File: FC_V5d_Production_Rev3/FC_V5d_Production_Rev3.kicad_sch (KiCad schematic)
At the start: 77 parts, among them IC3 RV-3028-C7_32.768kHz_1ppm_TA_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, J12 USB_C_Receptacle_USB2.0_16P, J16 DEBUG, J18 Payload, J22 SWD Port, J3 Life Makes Lemonade, J5 BM04B-SRSS-TB(LF)(SN), SW1 KMR2, SW2 KMR2, U12 TCA9548ARGERQ1, U14 TCA4307DGKR, U15 LIS2MDL, U2 ZDSD04GLGEAG, U30 E28-2G4M27S, U4 RFM98PW, U7 LSM6DSOTR

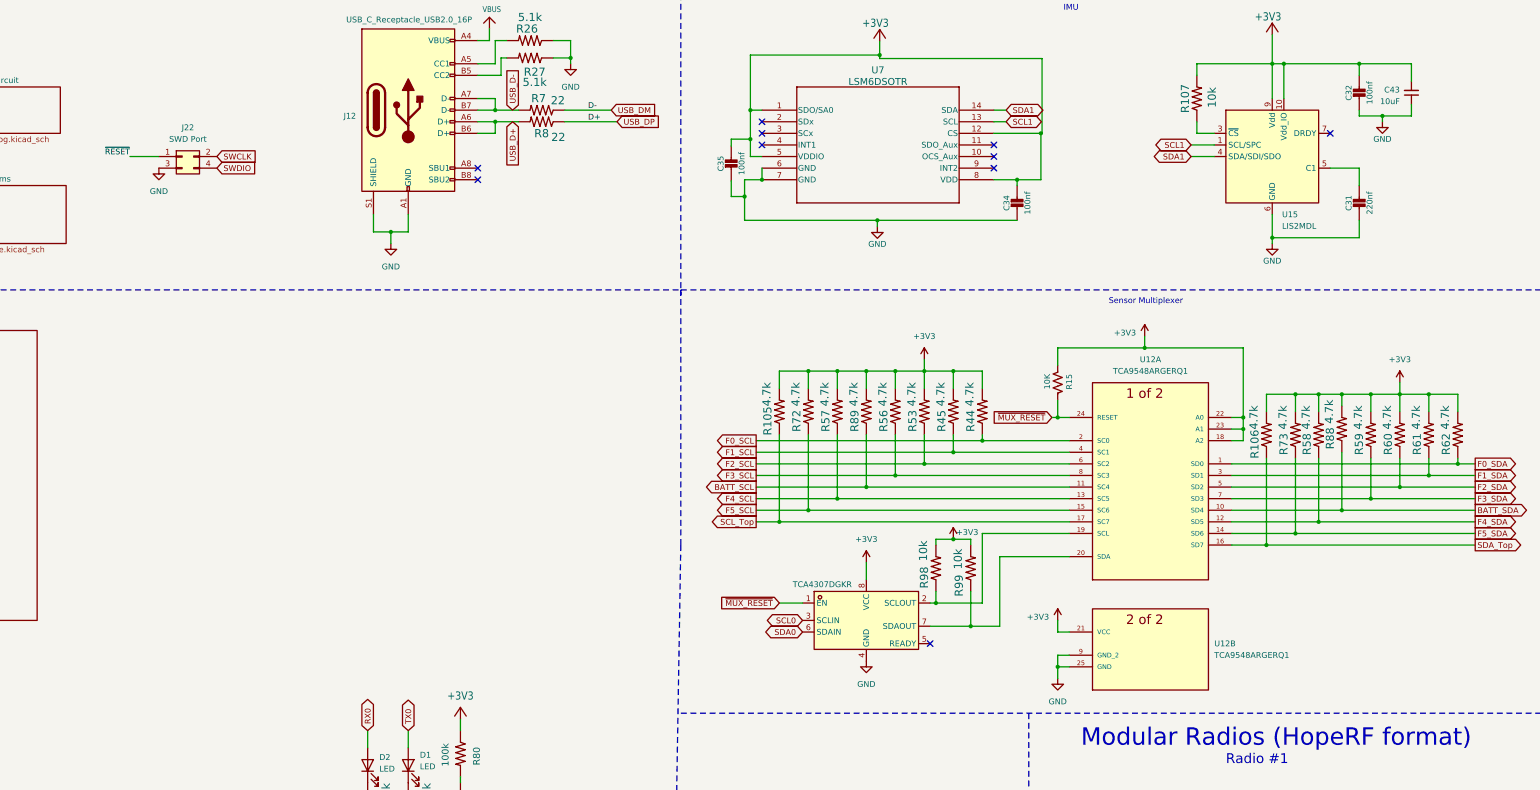
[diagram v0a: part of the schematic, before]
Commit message: Swapped to TCA With Leads
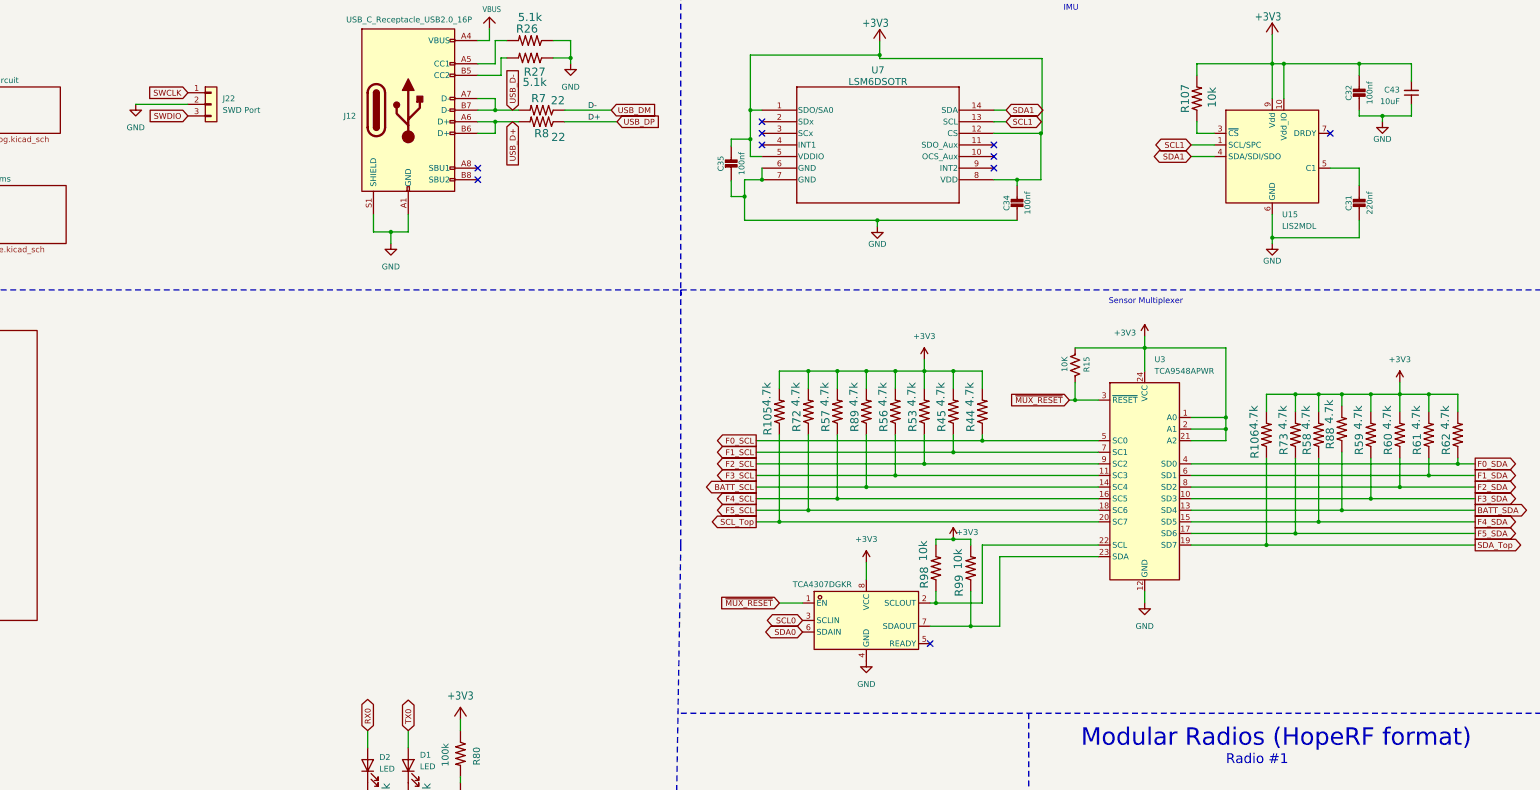
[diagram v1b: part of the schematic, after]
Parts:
- removed J22: SWD Port, Connector_PinHeader_1.27mm:PinHeader_2x02_P1.27mm_Vertical, symbol Connector_Generic:Conn_02x02_Odd_Even
- removed U12: TCA9548ARGERQ1, TCAQ1:QFN_GERQ1_TEX, symbol TCA9548ARGERQ1:TCA9548ARGERQ1
- added J22: SWD Port, Connector_JST:JST_SH_BM03B-SRSS-TB_1x03-1MP_P1.00mm_Vertical, symbol Connector_Generic:Conn_01x03
- added U3: TCA9548APWR, Package_SO:TSSOP-24_4.4x7.8mm_P0.65mm, symbol Interface_Expansion:TCA9548APWR
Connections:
- net +3V3: now also U3.1 (A0), U3.2 (A1), U3.21 (A2), U3.24 (VCC)
- net BATT_SCL: now also U3.14 (SC4)
- net BATT_SDA: now also U3.13 (SD4)
- net F0_SCL: now also U3.5 (SC0)
- net F0_SDA: now also U3.4 (SD0)
- net F1_SCL: now also U3.7 (SC1)
- net F1_SDA: now also U3.6 (SD1)
- net F2_SCL: now also U3.9 (SC2)
- net F2_SDA: now also U3.8 (SD2)
- net F3_SCL: now also U3.11 (SC3)
- net F3_SDA: now also U3.10 (SD3)
- net F4_SCL: now also U3.16 (SC5)
- net F4_SDA: now also U3.15 (SD5)
- net F5_SCL: now also U3.18 (SC6)
- net F5_SDA: now also U3.17 (SD6)
- net GND: now also J22.2 (Pin_2), U3.12 (GND)
- net SCL_Top: now also U3.20 (SC7)
- net SDA_Top: now also U3.19 (SD7)
- net SWCLK: now also J22.1 (Pin_1)
- net SWDIO: now also J22.3 (Pin_3)
- net ~{MUX_RESET}: now also U3.3 (~{RESET})
- net at R98.1, U14.2 (SCLOUT): now also U3.22 (SCL)
- net at R99.1, U14.7 (SDAOUT): now also U3.23 (SDA)
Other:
- moved on the sheet: R15

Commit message: Replaced RFM98PW with Ebyte E22-400M30
Also moved MCP GPIO Expander to I2C0 from I2C1.
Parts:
- removed JP7: SolderJumper_2_Open, Jumper:SolderJumper-2_P1.3mm_Open_RoundedPad1.0x1.5mm, symbol Jumper:SolderJumper_2_Open
- removed TP1: USBBOOT, TestPoint:TestPoint_Loop_D1.80mm_Drill1.0mm_Beaded, symbol Connector:TestPoint
- removed TP7: RESET, TestPoint:TestPoint_Loop_D1.80mm_Drill1.0mm_Beaded, symbol Connector:TestPoint
- removed U4: RFM98PW, FC_DEV_BOARD:RFM98PW, symbol mainboard:RFM98PW
- added R97: 10k, Resistor_SMD:R_0603_1608Metric, symbol mainboard:10KOHM-1_10W-1%(0603)0603
- added U13: E22-400M30S, easyeda2kicad:WIRELM-SMD_E22-400M30S, symbol easyeda2kicad:E22-400M30S
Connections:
- net +3V3: now also R97.1
- net GND: now also U13.1 (GND), U13.11 (GND), U13.12 (GND), U13.2 (GND), U13.20 (GND), U13.22 (GND), U13.3 (GND), U13.4 (GND), U13.5 (GND)
- net RF1_ANT: now also U13.21 (ANT)
- net RF1_IO0: now also U13.14 (BUSY)
- net RF1_RST: now also R97.2, U13.15 (NRST)
- net RF_VCC: now also U13.10 (VCC), U13.9 (VCC)
- net SPI0_CS0: now also U13.19 (NSS)
- net SPI0_MISO: now also U13.16 (MISO)
- net SPI0_MOSI: now also U13.17 (MOSI)
- net SPI0_SCK: now also U13.18 (SCK)
- net RF2_IO2: no longer names the net of U30.14 (DIO2)
- net RF2_IO3: no longer names the net of U30.15 (DIO3)
- new net RF1_IO1: U13.13 (DIO1)
- new net RF1_RX_EN: U13.6 (RXEN)
- new net RF1_TX_EN: U13.7 (TXEN)
- no-connect marks 17 -> 14
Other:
- moved on the sheet: R13, RF1
